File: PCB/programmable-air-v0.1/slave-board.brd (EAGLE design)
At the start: 101.5 x 50.8 mm, 18 parts, among them Q1 600mA/40V, Q2 600mA/40V, Q3 600mA/40V

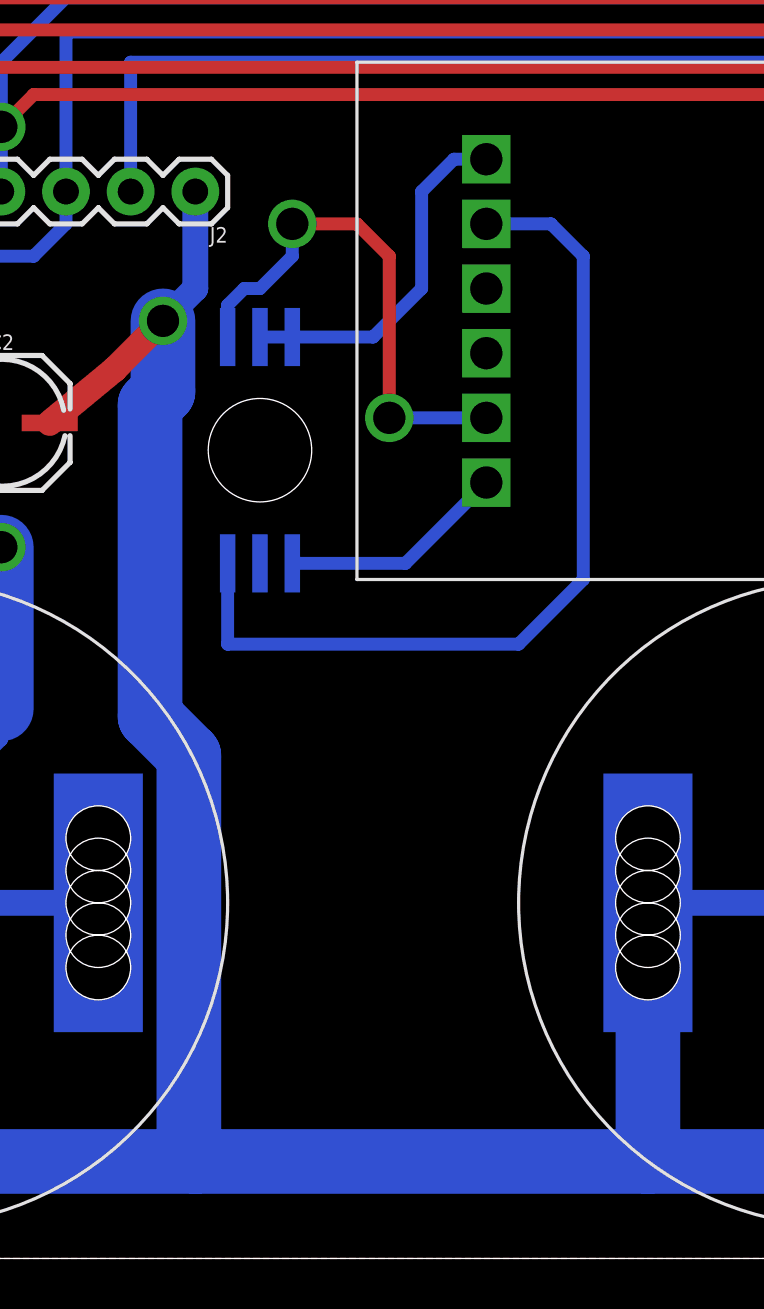
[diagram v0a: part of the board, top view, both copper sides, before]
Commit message: Modified slave board to have LM10CN
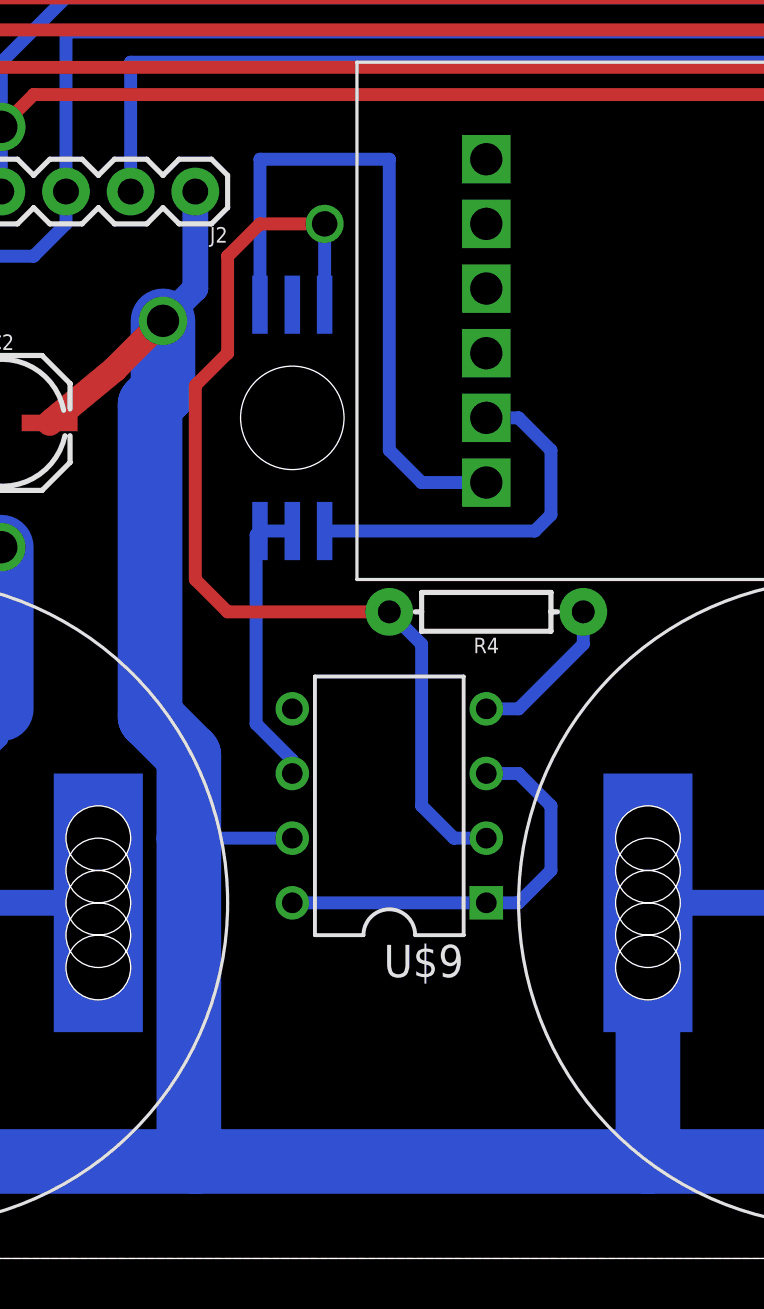
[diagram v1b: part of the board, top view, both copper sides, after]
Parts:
- added R4: (no value), SparkFun-Resistors:AXIAL-0.3
- added U$9: LM10CN, programmable-air-components:DIP8
- moved U$8 1.80 mm to (30.5, 33.0), turned to 90 degrees
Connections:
- removed net N$11: U$1.P$1, U$8.P$5, U$8.P$6
- new net N$16: U$8.P$5, U$8.P$6, U$9.6
- new net N$4: U$9.1, U$9.3, U$9.8
- net GND: now also R4.P$1, U$9.4
- net N$17: now also R4.P$2, U$9.2; no longer U$1.P$2
- net VIN: now also U$9.7
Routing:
- net N$21: track 8.94 -> 26.6 mm
- net N$4: track 0.00 -> 16.3 mm
- net N$11: track 14.0 -> 0.00 mm
- net N$16: track 0.00 -> 11.4 mm
- net GND: track 47.9 -> 54.1 mm
- net N$22: track 20.4 -> 14.8 mm, vias 2 -> 0
- net N$17: track 35.2 -> 40.1 mm, vias 0 -> 1
- net VIN: track 224.3 -> 228.4 mm
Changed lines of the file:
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@@
 <layers>
 <layer number="1" name="Top" color="4" fill="1" visible="yes" active="yes"/>
+<layer number="2" name="Route2" color="1" fill="3" visible="no" active="yes"/>
+<layer number="3" name="Route3" color="4" fill="3" visible="no" active="yes"/>
+<layer number="4" name="Route4" color="1" fill="4" visible="no" active="yes"/>
+<layer number="5" name="Route5" color="4" fill="4" visible="no" active="yes"/>
+<layer number="6" name="Route6" color="1" fill="8" visible="no" active="yes"/>
+<layer number="7" name="Route7" color="4" fill="8" visible="no" active="yes"/>
+<layer number="8" name="Route8" color="1" fill="2" visible="no" active="yes"/>
+<layer number="9" name="Route9" color="4" fill="2" visible="no" active="yes"/>
+<layer number="10" name="Route10" color="1" fill="7" visible="no" active="yes"/>
+<layer number="11" name="Route11" color="4" fill="7" visible="no" active="yes"/>
+<layer number="12" name="Route12" color="1" fill="5" visible="no" active="yes"/>
+<layer number="13" name="Route13" color="4" fill="5" visible="no" active="yes"/>
+<layer number="14" name="Route14" color="1" fill="6" visible="no" active="yes"/>
+<layer number="15" name="Route15" color="4" fill="6" visible="no" active="yes"/>
 <layer number="16" name="Bottom" color="1" fill="1" visible="yes" active="yes"/>
 <layer number="17" name="Pads" color="2" fill="1" visible="yes" active="yes"/>
@@
 <element name="U$6" library="programmable-air-components" package="IN4148" value="IN4148" x="15.24" y="13.97" rot="MR0"/>
 <element name="U$7" library="programmable-air-components" package="IN4148" value="IN4148" x="86.36" y="13.97" rot="MR0"/>
-<element name="U$8" library="programmable-air-components" package="2SMPP-03" value="2SMPP-03" x="29.21" y="31.75" rot="R270"/>
+<element name="U$8" library="programmable-air-components" package="2SMPP-03" value="2SMPP-03" x="30.48" y="33.02" rot="R90"/>
+<element name="U$9" library="programmable-air-components" package="DIP8" value="LM10CN" x="34.29" y="17.78" rot="R90"/>
+<element name="R4" library="SparkFun-Resistors" package="AXIAL-0.3" value=" " x="38.1" y="25.4" rot="R180">
+<attribute name="PROD_ID" value=" " x="38.1" y="25.4" size="1.778" layer="27" rot="R180" display="off"/>
+</element>
 </elements>
 <signals>
@@
 <wire x1="24.892" y1="21.28246875" x2="26.416" y2="19.75846875" width="2.54" layer="16"/>
 <wire x1="26.416" y1="4.064" x2="26.67" y2="3.81" width="2.54" layer="16"/>
-<wire x1="26.416" y1="19.75846875" x2="26.416" y2="4.064" width="2.54" layer="16"/>
+<wire x1="26.416" y1="16.51" x2="26.416" y2="19.75846875" width="2.54" layer="16"/>
+<wire x1="26.416" y1="16.51" x2="26.416" y2="4.064" width="2.54" layer="16"/>
 <wire x1="78.74" y1="13.97" x2="84.5312" y2="13.97" width="1.016" layer="16"/>
 <wire x1="44.45" y1="13.97" x2="50.2412" y2="13.97" width="1.016" layer="16"/>
@@
 <wire x1="78.74" y1="13.97" x2="78.74" y2="3.81" width="2.54" layer="16"/>
 <wire x1="92.71" y1="40.64" x2="97.79" y2="40.64" width="1.27" layer="16"/>
+<contactref element="U$9" pad="7"/>
+<wire x1="30.48" y1="16.51" x2="26.416" y2="16.51" width="0.508" layer="16"/>
 </signal>
 <signal name="GND">
@@
 <via x="8.89" y="39.37" extent="1-16" drill="1.27"/>
 <wire x1="8.89" y1="39.37" x2="8.89" y2="41.91" width="1.016" layer="16"/>
+<contactref element="U$9" pad="4"/>
+<contactref element="R4" pad="P$1"/>
+<wire x1="39.37" y1="21.59" x2="38.1" y2="21.59" width="0.508" layer="16"/>
+<wire x1="39.37" y1="21.59" x2="41.91" y2="24.13" width="0.508" layer="16"/>
+<wire x1="41.91" y1="24.13" x2="41.91" y2="25.4" width="0.508" layer="16"/>
+</signal>
+<signal name="N$16">
+<contactref element="U$8" pad="P$6"/>
+<contactref element="U$8" pad="P$5"/>
+<wire x1="29.21" y1="28.575" x2="30.48" y2="28.575" width="0.508" layer="16"/>
+<contactref element="U$9" pad="6"/>
+<wire x1="30.48" y1="19.05" x2="30.48" y2="19.57841875" width="0.508" layer="16"/>
+<wire x1="30.48" y1="19.57841875" x2="29.0576" y2="21.00081875" width="0.508" layer="16"/>
+<wire x1="29.0576" y1="28.4226" x2="29.21" y2="28.575" width="0.508" layer="16"/>
+<wire x1="29.0576" y1="21.00081875" x2="29.0576" y2="28.4226" width="0.508" layer="16"/>
 </signal>
 <signal name="N$4">
+<contactref element="U$9" pad="8"/>
+<contactref element="U$9" pad="1"/>
+<contactref element="U$9" pad="3"/>
+<wire x1="38.1" y1="13.97" x2="39.37" y2="13.97" width="0.508" layer="16"/>
+<wire x1="39.37" y1="13.97" x2="40.64" y2="15.24" width="0.508" layer="16"/>
+<wire x1="40.64" y1="15.24" x2="40.64" y2="17.78" width="0.508" layer="16"/>
+<wire x1="40.64" y1="17.78" x2="39.37" y2="19.05" width="0.508" layer="16"/>
+<wire x1="39.37" y1="19.05" x2="38.1" y2="19.05" width="0.508" layer="16"/>
+<wire x1="30.48" y1="13.97" x2="38.1" y2="13.97" width="0.508" layer="16"/>
+</signal>
+<signal name="N$17">
+<contactref element="U$9" pad="2"/>
+<contactref element="R4" pad="P$2"/>
+<contactref element="U$8" pad="P$3"/>
+<wire x1="38.1" y1="16.51" x2="36.83" y2="16.51" width="0.508" layer="16"/>
+<wire x1="36.83" y1="16.51" x2="35.56" y2="17.78" width="0.508" layer="16"/>
+<wire x1="35.56" y1="17.78" x2="35.56" y2="24.13" width="0.508" layer="16"/>
+<wire x1="35.56" y1="24.13" x2="34.29" y2="25.4" width="0.508" layer="16"/>
+<wire x1="31.75" y1="37.465" x2="31.75" y2="40.64" width="0.508" layer="16"/>
+<via x="31.75" y="40.64" extent="1-16" drill="1"/>
+<wire x1="31.75" y1="40.64" x2="29.21" y2="40.64" width="0.508" layer="1"/>
+<wire x1="29.21" y1="40.64" x2="27.94" y2="39.37" width="0.508" layer="1"/>
+<wire x1="27.94" y1="39.37" x2="27.94" y2="35.56" width="0.508" layer="1"/>
+<wire x1="27.94" y1="35.56" x2="26.67" y2="34.29" width="0.508" layer="1"/>
+<wire x1="26.67" y1="34.29" x2="26.67" y2="26.67" width="0.508" layer="1"/>
+<wire x1="26.67" y1="26.67" x2="27.94" y2="25.4" width="0.508" layer="1"/>
+<wire x1="27.94" y1="25.4" x2="34.29" y2="25.4" width="0.508" layer="1"/>
+</signal>
+<signal name="N$21">
 <contactref element="U$8" pad="P$1"/>
 <contactref element="U$1" pad="P$6"/>
-<wire x1="30.48" y1="27.305" x2="34.925" y2="27.305" width="0.508" layer="16"/>
-<wire x1="34.925" y1="27.305" x2="38.1" y2="30.48" width="0.508" layer="16"/>
-</signal>
-<signal name="N$6">
+<wire x1="29.21" y1="37.465" x2="29.21" y2="43.18" width="0.508" layer="16"/>
+<wire x1="29.21" y1="43.18" x2="34.29" y2="43.18" width="0.508" layer="16"/>
+<wire x1="34.29" y1="43.18" x2="34.29" y2="31.75" width="0.508" layer="16"/>
+<wire x1="34.29" y1="31.75" x2="35.56" y2="30.48" width="0.508" layer="16"/>
+<wire x1="35.56" y1="30.48" x2="38.1" y2="30.48" width="0.508" layer="16"/>
+</signal>
+<signal name="N$22">
+<contactref element="U$8" pad="P$4"/>
 <contactref element="U$1" pad="P$5"/>
-<contactref element="U$8" pad="P$4"/>
-<wire x1="28.58956875" y1="38.1" x2="29.21" y2="38.1" width="0.508" layer="16"/>
-<wire x1="29.21" y1="38.1" x2="30.48" y2="39.37" width="0.508" layer="16"/>
-<wire x1="27.94" y1="36.195" x2="27.94" y2="37.45043125" width="0.508" layer="16"/>
-<wire x1="27.94" y1="37.45043125" x2="28.58956875" y2="38.1" width="0.508" layer="16"/>
-<wire x1="30.48" y1="39.37" x2="30.48" y2="40.64" width="0.508" layer="16"/>
-<via x="30.48" y="40.64" extent="1-16" drill="1.27"/>
-<wire x1="33.02" y1="40.64" x2="34.29" y2="39.37" width="0.508" layer="1"/>
-<wire x1="34.29" y1="39.37" x2="34.29" y2="33.02" width="0.508" layer="1"/>
-<via x="34.29" y="33.02" extent="1-16" drill="1.27"/>
-<wire x1="34.29" y1="33.02" x2="38.1" y2="33.02" width="0.508" layer="16"/>
-<wire x1="30.48" y1="40.64" x2="33.02" y2="40.64" width="0.508" layer="1"/>
-</signal>
-<signal name="N$11">
-<contactref element="U$8" pad="P$6"/>
-<contactref element="U$8" pad="P$5"/>
-<wire x1="29.21" y1="36.195" x2="30.48" y2="36.195" width="0.508" layer="16"/>
-<wire x1="30.48" y1="36.195" x2="33.655" y2="36.195" width="0.508" layer="16"/>
-<wire x1="33.655" y1="36.195" x2="35.56" y2="38.1" width="0.508" layer="16"/>
-<contactref element="U$1" pad="P$1"/>
-<wire x1="35.56" y1="38.1" x2="35.56" y2="41.91" width="0.508" layer="16"/>
-<wire x1="35.56" y1="41.91" x2="36.83" y2="43.18" width="0.508" layer="16"/>
-<wire x1="36.83" y1="43.18" x2="38.1" y2="43.18" width="0.508" layer="16"/>
-</signal>
-<signal name="N$17">
-<contactref element="U$1" pad="P$2"/>
-<contactref element="U$8" pad="P$3"/>
-<wire x1="40.64" y1="40.64" x2="41.91" y2="39.37" width="0.508" layer="16"/>
-<wire x1="39.37" y1="24.13" x2="27.94" y2="24.13" width="0.508" layer="16"/>
-<wire x1="27.94" y1="24.13" x2="27.94" y2="27.305" width="0.508" layer="16"/>
-<wire x1="38.1" y1="40.64" x2="40.64" y2="40.64" width="0.508" layer="16"/>
-<wire x1="41.91" y1="39.37" x2="41.91" y2="26.67" width="0.508" layer="16"/>
-<wire x1="41.91" y1="26.67" x2="39.37" y2="24.13" width="0.508" layer="16"/>
+<wire x1="31.75" y1="28.575" x2="40.005" y2="28.575" width="0.508" layer="16"/>
+<wire x1="40.005" y1="28.575" x2="40.64" y2="29.21" width="0.508" layer="16"/>
+<wire x1="40.64" y1="29.21" x2="40.64" y2="31.75" width="0.508" layer="16"/>
+<wire x1="40.64" y1="31.75" x2="39.37" y2="33.02" width="0.508" layer="16"/>
+<wire x1="39.37" y1="33.02" x2="38.1" y2="33.02" width="0.508" layer="16"/>
 </signal>
 </signals>

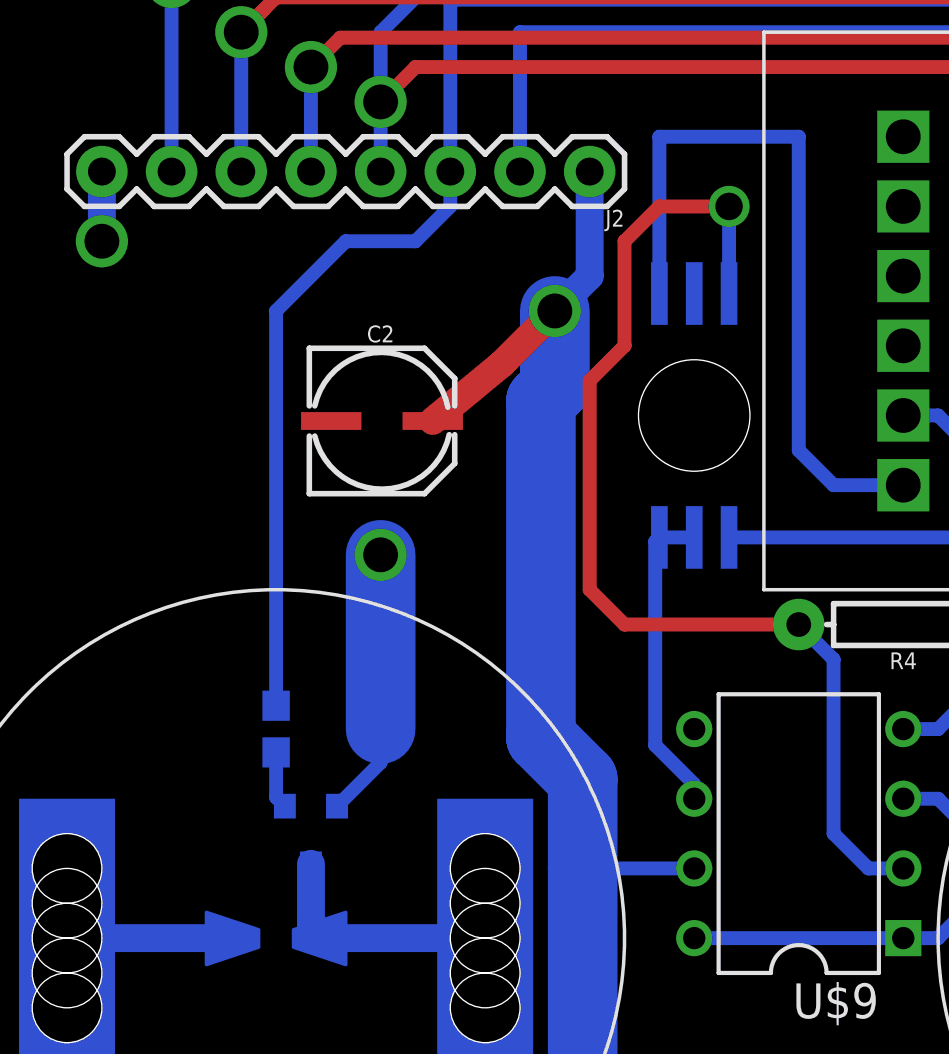
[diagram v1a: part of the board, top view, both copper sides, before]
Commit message: Added PCB for testing SMPP with LM10 and HX711. Added gitignore.
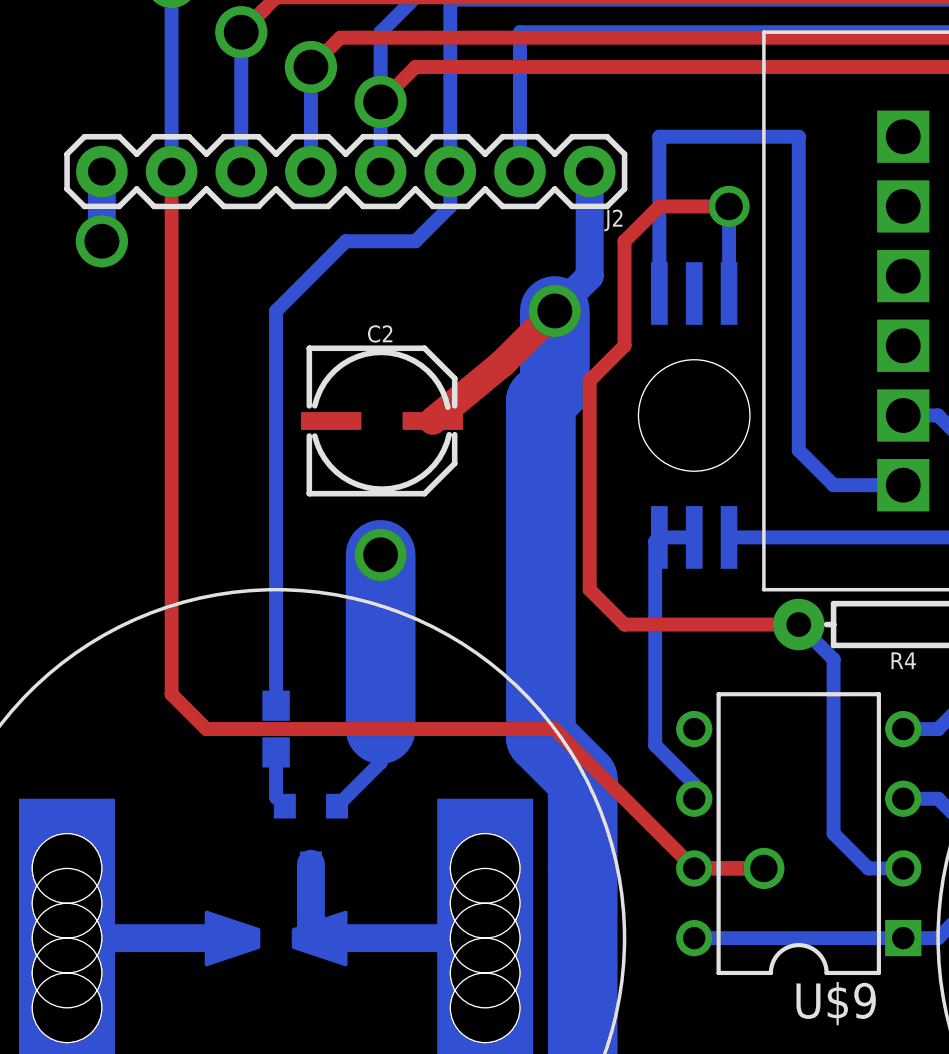
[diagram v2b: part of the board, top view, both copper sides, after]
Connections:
- net N$15: now also U$9.7
- net VIN: no longer U$9.7
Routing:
- net N$15: track 110.1 -> 156.0 mm, vias 4 -> 5
- net VIN: track 228.4 -> 224.3 mm
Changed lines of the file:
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@@
 <wire x1="77.47" y1="40.64" x2="77.47" y2="43.18" width="0.6096" layer="16"/>
 <wire x1="77.47" y1="43.18" x2="77.47" y2="40.64" width="0.6096" layer="1"/>
+<contactref element="U$9" pad="7"/>
+<wire x1="11.43" y1="41.91" x2="11.43" y2="22.86" width="0.508" layer="1"/>
+<wire x1="11.43" y1="22.86" x2="12.7" y2="21.59" width="0.508" layer="1"/>
+<wire x1="12.7" y1="21.59" x2="25.4" y2="21.59" width="0.508" layer="1"/>
+<wire x1="25.4" y1="21.59" x2="30.48" y2="16.51" width="0.508" layer="1"/>
+<via x="33.02" y="16.51" extent="1-16" drill="1"/>
+<wire x1="33.02" y1="16.51" x2="30.48" y2="16.51" width="0.508" layer="16"/>
+<wire x1="30.48" y1="16.51" x2="33.02" y2="16.51" width="0.508" layer="1"/>
 </signal>
 <signal name="VIN">
@@
 <wire x1="78.74" y1="13.97" x2="78.74" y2="3.81" width="2.54" layer="16"/>
 <wire x1="92.71" y1="40.64" x2="97.79" y2="40.64" width="1.27" layer="16"/>
-<contactref element="U$9" pad="7"/>
-<wire x1="30.48" y1="16.51" x2="26.416" y2="16.51" width="0.508" layer="16"/>
 </signal>
 <signal name="GND">
